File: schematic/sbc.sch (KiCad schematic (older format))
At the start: 15 parts

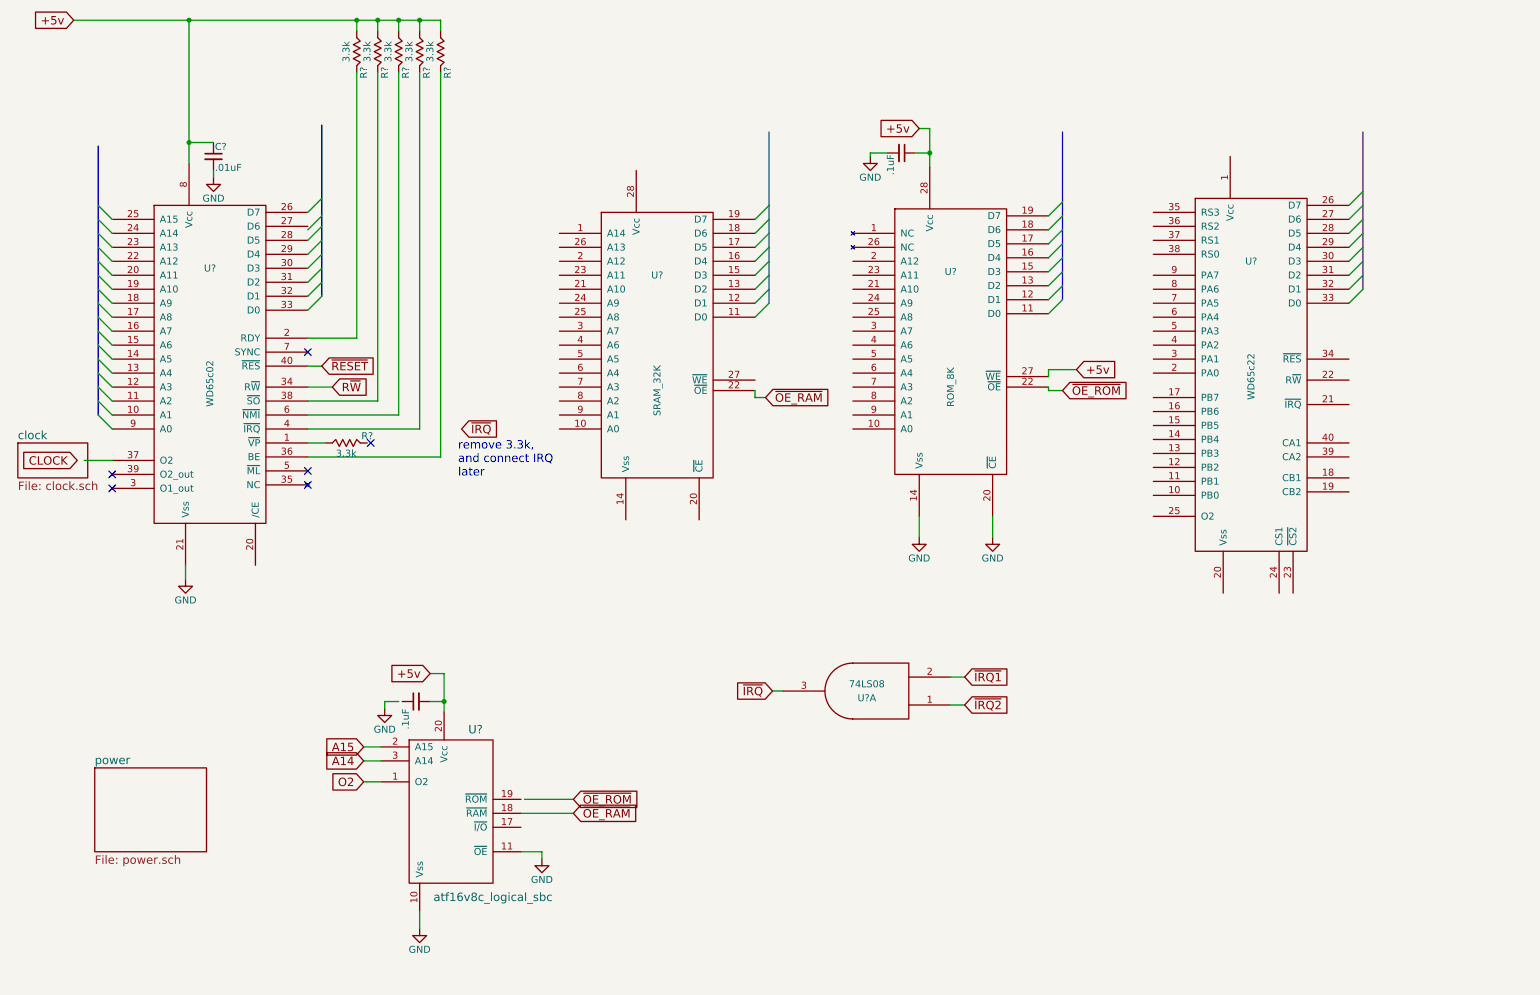
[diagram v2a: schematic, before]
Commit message: sbc schematic update. Wired in RAM
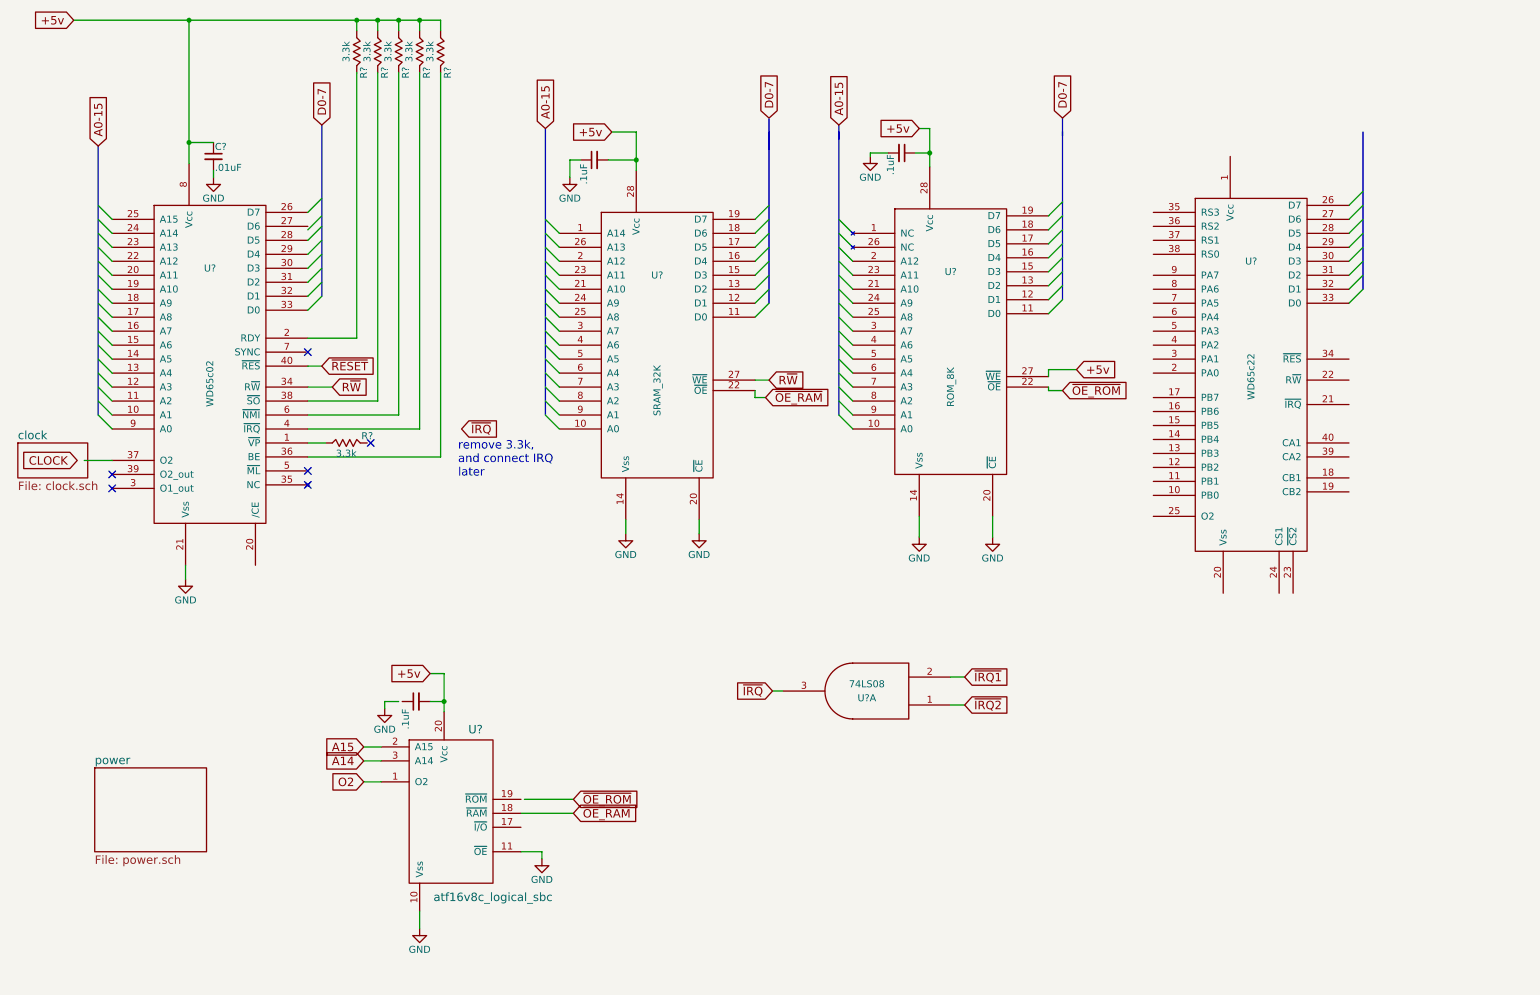
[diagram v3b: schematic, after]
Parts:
- added C?: .1uF, symbol C_Small
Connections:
- net labels added: A0-15, D0-7
- wire segments 53 -> 61
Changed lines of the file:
@@
 Text GLabel 5825 3475 2    60   Input ~ 0
 ~OE_RAM~
-Wire Bus Line
-	10100 1575 10100 2700
-Wire Bus Line
-	7950 1575 7950 2775
-Wire Bus Line
-	5850 1575 5850 2800
-Wire Bus Line
-	2650 1525 2650 2750
-Wire Wire Line
-	5875 5575 5950 5575
-Wire Wire Line
-	7150 5475 7250 5475
-Wire Wire Line
-	7150 5675 7250 5675
-Wire Wire Line
-	3350 3700 3350 1150
-Wire Wire Line
-	2550 3600 3200 3600
-Wire Wire Line
-	3200 3600 3200 1150
-Wire Wire Line
-	2550 3050 2900 3050
-Wire Wire Line
-	2550 3500 3050 3500
-Wire Wire Line
-	3050 3500 3050 1150
-Wire Wire Line
-	2550 3400 2725 3400
-Wire Wire Line
-	2550 3250 2650 3250
-Wire Wire Line
-	1700 1800 1700 775
-Wire Wire Line
-	875  775  3500 775
-Connection ~ 1700 775
-Wire Wire Line
-	2900 3050 2900 1150
-Wire Wire Line
-	3500 775  3500 850
-Wire Wire Line
-	3350 850  3350 775
-Connection ~ 3350 775
-Connection ~ 3200 775
-Wire Wire Line
-	3050 850  3050 775
-Connection ~ 3050 775
-Wire Wire Line
-	2900 850  2900 775
-Connection ~ 2900 775
-Wire Wire Line
-	3200 850  3200 775
-Wire Bus Line
-	1050 3600 1050 1675
-Wire Wire Line
-	950  3925 1150 3925
-Wire Wire Line
-	1675 4775 1675 4675
-Wire Wire Line
-	1875 1650 1700 1650
-Connection ~ 1700 1650
-Wire Wire Line
-	1875 1900 1875 1850
-Wire Wire Line
-	2550 3800 2675 3800
-Wire Wire Line
-	2550 3900 3500 3900
-Wire Wire Line
-	3500 3900 3500 1150
-Wire Wire Line
-	2550 3700 3350 3700
-Wire Wire Line
-	4100 6350 4450 6350
-Wire Wire Line
-	4075 6450 4450 6450
-Wire Wire Line
-	7950 3425 7850 3425
-Wire Wire Line
-	7850 3425 7850 3400
-Wire Wire Line
-	5750 3425 5750 3475
-Wire Wire Line
-	5750 3475 5825 3475
 $Comp
 L GND #PWR?
@@
 	1    0    0    -1
 $EndComp
-Wire Wire Line
-	3350 7275 3350 7150
-Wire Wire Line
-	4075 6725 4225 6725
-Wire Wire Line
-	4225 6725 4225 6775
 Text GLabel 3425 5450 0    60   Input ~ 0
 +5v
@@
 	0    -1   -1   0
 $EndComp
-Wire Wire Line
-	3425 5450 3525 5450
-Wire Wire Line
-	3525 5450 3525 5725
-Wire Wire Line
-	3425 5650 3525 5650
-Connection ~ 3525 5650
 $Comp
 L GND #PWR?
@@
 	1    0    0    -1
 $EndComp
-Wire Wire Line
-	3200 5650 3100 5650
-Wire Wire Line
-	3100 5650 3100 5700
 Text GLabel 2950 5975 0    60   Input ~ 0
 A15
 Text GLabel 2950 6075 0    60   Input ~ 0
 A14
-Wire Wire Line
-	2950 5975 3075 5975
-Wire Wire Line
-	2950 6075 3075 6075
 Text GLabel 2950 6225 0    60   Input ~ 0
 O2
-Wire Wire Line
-	2950 6225 3075 6225
 Text GLabel 6925 1550 0    60   Input ~ 0
 +5v
@@
 	1    0    0    -1
 $EndComp
-Wire Wire Line
-	6925 1550 7000 1550
-Wire Wire Line
-	7000 1550 7000 1825
-Wire Wire Line
-	6900 1725 7000 1725
-Connection ~ 7000 1725
-Wire Wire Line
-	6700 1725 6575 1725
-Wire Wire Line
-	6575 1725 6575 1750
 $Comp
 L GND #PWR?
@@
 	1    0    0    -1
 $EndComp
-Wire Wire Line
-	7450 4475 7450 4325
-Wire Wire Line
-	6925 4475 6925 4325
 Text GLabel 8050 3275 2    60   Input ~ 0
 +5v
+$Comp
+L GND #PWR?
+U 1 1 5830B7BE
+P 5350 4450
+F 0 "#PWR?" H 5350 4200 50  0001 C CNN
+F 1 "GND" H 5350 4300 50  0000 C CNN
+F 2 "" H 5350 4450 50  0000 C CNN
+F 3 "" H 5350 4450 50  0000 C CNN
+	1    5350 4450
+	1    0    0    -1
+$EndComp
+$Comp
+L GND #PWR?
+U 1 1 5830B7F9
+P 4825 4450
+F 0 "#PWR?" H 4825 4200 50  0001 C CNN
+F 1 "GND" H 4825 4300 50  0000 C CNN
+F 2 "" H 4825 4450 50  0000 C CNN
+F 3 "" H 4825 4450 50  0000 C CNN
+	1    4825 4450
+	1    0    0    -1
+$EndComp
+Text GLabel 5850 3350 2    60   Input ~ 0
+R~W~
+Text GLabel 4725 1575 0    60   Input ~ 0
++5v
+$Comp
+L C_Small C?
+U 1 1 5830BB33
+P 4600 1775
+F 0 "C?" H 4610 1845 50  0001 L CNN
+F 1 ".1uF" H 4425 1850 50  0000 L CNN
+F 2 "" H 4600 1775 50  0000 C CNN
+F 3 "" H 4600 1775 50  0000 C CNN
+	1    4600 1775
+	0    -1   -1   0
+$EndComp
+$Comp
+L GND #PWR?
+U 1 1 5830BC6D
+P 4425 1900
+F 0 "#PWR?" H 4425 1650 50  0001 C CNN
+F 1 "GND" H 4425 1750 50  0000 C CNN
+F 2 "" H 4425 1900 50  0000 C CNN
+F 3 "" H 4425 1900 50  0000 C CNN
+	1    4425 1900
+	1    0    0    -1
+$EndComp
+Entry Wire Line
+	4250 2200 4350 2300
+Entry Wire Line
+	4250 2300 4350 2400
+Entry Wire Line
+	4250 2400 4350 2500
+Entry Wire Line
+	4250 2500 4350 2600
+Entry Wire Line
+	4250 2600 4350 2700
+Entry Wire Line
+	4250 2700 4350 2800
+Entry Wire Line
+	4250 2800 4350 2900
+Entry Wire Line
+	4250 2900 4350 3000
+Entry Wire Line
+	4250 3000 4350 3100
+Entry Wire Line
+	4250 3100 4350 3200
+Entry Wire Line
+	4250 3200 4350 3300
+Entry Wire Line
+	4250 3300 4350 3400
+Entry Wire Line
+	4250 3400 4350 3500
+Entry Wire Line
+	4250 3500 4350 3600
+Entry Wire Line
+	4250 3600 4350 3700
+Entry Wire Line
+	6350 2200 6450 2300
+Entry Wire Line
+	6350 2300 6450 2400
+Entry Wire Line
+	6350 2400 6450 2500
+Entry Wire Line
+	6350 2500 6450 2600
+Entry Wire Line
+	6350 2600 6450 2700
+Entry Wire Line
+	6350 2700 6450 2800
+Entry Wire Line
+	6350 2800 6450 2900
+Entry Wire Line
+	6350 2900 6450 3000
+Entry Wire Line
+	6350 3000 6450 3100
+Entry Wire Line
+	6350 3100 6450 3200
+Entry Wire Line
+	6350 3200 6450 3300
+Entry Wire Line
+	6350 3300 6450 3400
+Entry Wire Line
+	6350 3400 6450 3500
+Entry Wire Line
+	6350 3500 6450 3600
+Entry Wire Line
+	6350 3600 6450 3700
+Text GLabel 6350 1525 1    60   Input ~ 0
+A0-15
+Text GLabel 4250 1550 1    60   Input ~ 0
+A0-15
+Text GLabel 1050 1675 1    60   Input ~ 0
+A0-15
+Text GLabel 5850 1475 1    60   Input ~ 0
+D0-7
+Text GLabel 7950 1475 1    60   Input ~ 0
+D0-7
+Text GLabel 2650 1525 1    60   Input ~ 0
+D0-7
+Wire Bus Line
+	10100 1575 10100 2700
+Wire Bus Line
+	7950 1575 7950 2775
+Wire Bus Line
+	5850 1575 5850 2800
+Wire Bus Line
+	2650 1525 2650 2750
+Wire Wire Line
+	5875 5575 5950 5575
+Wire Wire Line
+	7150 5475 7250 5475
+Wire Wire Line
+	7150 5675 7250 5675
+Wire Wire Line
+	3350 3700 3350 1150
+Wire Wire Line
+	2550 3600 3200 3600
+Wire Wire Line
+	3200 3600 3200 1150
+Wire Wire Line
+	2550 3050 2900 3050
+Wire Wire Line
+	2550 3500 3050 3500
+Wire Wire Line
+	3050 3500 3050 1150
+Wire Wire Line
+	2550 3400 2725 3400
+Wire Wire Line
+	2550 3250 2650 3250
+Wire Wire Line
+	1700 1800 1700 775
+Wire Wire Line
+	875  775  3500 775
+Connection ~ 1700 775
+Wire Wire Line
+	2900 3050 2900 1150
+Wire Wire Line
+	3500 775  3500 850
+Wire Wire Line
+	3350 850  3350 775
+Connection ~ 3350 775
+Connection ~ 3200 775
+Wire Wire Line
+	3050 850  3050 775
+Connection ~ 3050 775
+Wire Wire Line
+	2900 850  2900 775
+Connection ~ 2900 775
+Wire Wire Line
+	3200 850  3200 775
+Wire Bus Line
+	1050 3600 1050 1675
+Wire Wire Line
+	950  3925 1150 3925
+Wire Wire Line
+	1675 4775 1675 4675
+Wire Wire Line
+	1875 1650 1700 1650
+Connection ~ 1700 1650
+Wire Wire Line
+	1875 1900 1875 1850
+Wire Wire Line
+	2550 3800 2675 3800
+Wire Wire Line
+	2550 3900 3500 3900
+Wire Wire Line
+	3500 3900 3500 1150
+Wire Wire Line
+	2550 3700 3350 3700
+Wire Wire Line
+	4100 6350 4450 6350
+Wire Wire Line
+	4075 6450 4450 6450
+Wire Wire Line
+	7950 3425 7850 3425
+Wire Wire Line
+	7850 3425 7850 3400
+Wire Wire Line
+	5750 3425 5750 3475
+Wire Wire Line
+	5750 3475 5825 3475
+Wire Wire Line
+	3350 7275 3350 7150
+Wire Wire Line
+	4075 6725 4225 6725
+Wire Wire Line
+	4225 6725 4225 6775
+Wire Wire Line
+	3425 5450 3525 5450
+Wire Wire Line
+	3525 5450 3525 5725
+Wire Wire Line
+	3425 5650 3525 5650
+Connection ~ 3525 5650
+Wire Wire Line
+	3200 5650 3100 5650
+Wire Wire Line
+	3100 5650 3100 5700
+Wire Wire Line
+	2950 5975 3075 5975
+Wire Wire Line
+	2950 6075 3075 6075
+Wire Wire Line
+	2950 6225 3075 6225
+Wire Wire Line
+	6925 1550 7000 1550
+Wire Wire Line
+	7000 1550 7000 1825
+Wire Wire Line
+	6900 1725 7000 1725
+Connection ~ 7000 1725
+Wire Wire Line
+	6700 1725 6575 1725
+Wire Wire Line
+	6575 1725 6575 1750
+Wire Wire Line
+	7450 4475 7450 4325
+Wire Wire Line
+	6925 4475 6925 4325
 Wire Wire Line
 	7850 3325 7850 3275
 Wire Wire Line
 	7850 3275 8050 3275
+Wire Wire Line
+	5350 4450 5350 4350
+Wire Wire Line
+	4825 4450 4825 4350
+Wire Wire Line
+	5750 3350 5850 3350
+Wire Wire Line
+	4725 1575 4900 1575
+Wire Wire Line
+	4900 1575 4900 1850
+Wire Wire Line
+	4700 1775 4900 1775
+Connection ~ 4900 1775
+Wire Bus Line
+	6350 3600 6350 1575
+Wire Wire Line
+	4425 1900 4425 1775
+Wire Wire Line
+	4425 1775 4500 1775
+Wire Bus Line
+	4250 3600 4250 1550
+Wire Bus Line
+	6350 1525 6350 1625
+Wire Bus Line
+	5850 1475 5850 1700
+Wire Bus Line
+	7950 1475 7950 1600
 $EndSCHEMATC

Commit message: Added 65c22 basic connections to schematic
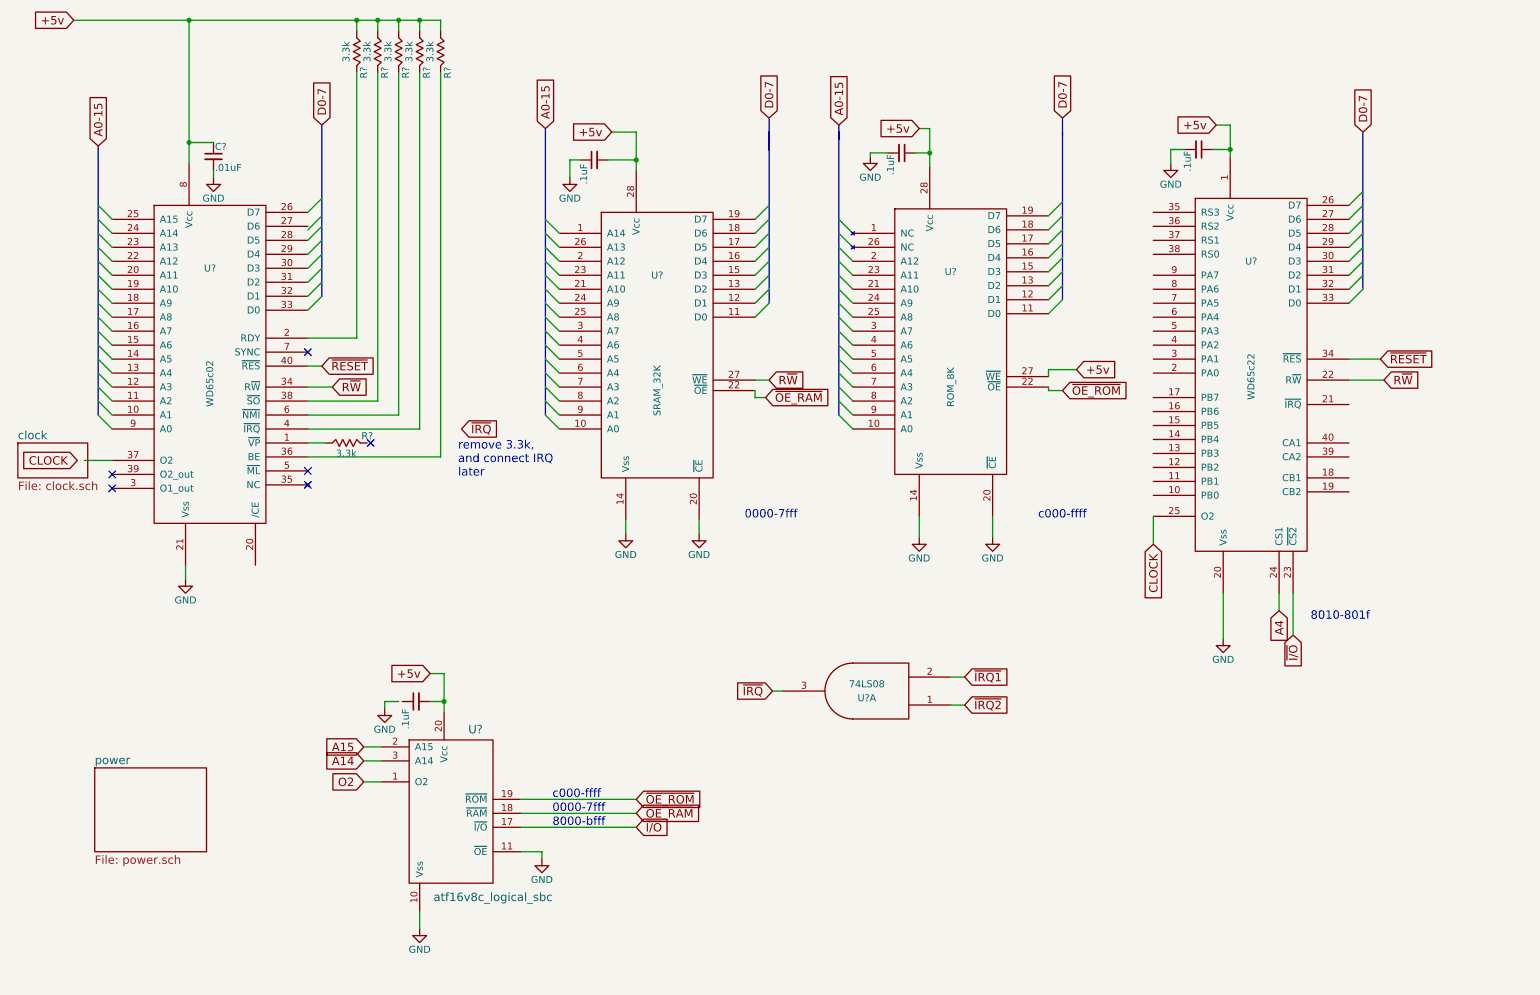
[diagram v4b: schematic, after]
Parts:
- added C?: .1uF, symbol C_Small
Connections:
- net labels added: A4, ~I/O~
- wire segments 61 -> 73
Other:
- note added: "0000-7fff"
- note added: "8000-bfff"
- note added: "8010-801f"
- note added: "c000-ffff"
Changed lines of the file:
@@
 	1    0    0    -1
 $EndComp
-Text GLabel 4450 6350 2    60   Input ~ 0
+Text GLabel 4900 6350 2    60   Input ~ 0
 ~OE_ROM~
-Text GLabel 4450 6450 2    60   Input ~ 0
+Text GLabel 4900 6450 2    60   Input ~ 0
 ~OE_RAM~
 Text GLabel 7950 3425 2    60   Input ~ 0
@@
 	2550 3700 3350 3700
 Wire Wire Line
-	4100 6350 4450 6350
-Wire Wire Line
-	4075 6450 4450 6450
+	4075 6450 4900 6450
 Wire Wire Line
 	7950 3425 7850 3425
@@
 Wire Bus Line
 	7950 1475 7950 1600
+Text GLabel 9500 5000 3    60   Input ~ 0
+A4
+Wire Wire Line
+	9500 5000 9500 4875
+Text GLabel 9600 5175 3    60   Input ~ 0
+~I/O~
+Wire Wire Line
+	9600 5175 9600 4875
+Text GLabel 4900 6550 2    60   Input ~ 0
+~I/O~
+Wire Wire Line
+	4075 6550 4900 6550
+Wire Wire Line
+	4075 6350 4900 6350
+Text Notes 9725 5075 0    60   ~ 0
+8010-801f
+Text Notes 7775 4350 0    60   ~ 0
+c000-ffff
+Text Notes 5675 4350 0    60   ~ 0
+0000-7fff
+Text Notes 4300 6350 0    60   ~ 0
+c000-ffff
+Text Notes 4300 6450 0    60   ~ 0
+0000-7fff
+Text Notes 4300 6550 0    60   ~ 0
+8000-bfff
+$Comp
+L GND #PWR?
+U 1 1 58336CFD
+P 9100 5200
+F 0 "#PWR?" H 9100 4950 50  0001 C CNN
+F 1 "GND" H 9100 5050 50  0000 C CNN
+F 2 "" H 9100 5200 50  0000 C CNN
+F 3 "" H 9100 5200 50  0000 C CNN
+	1    9100 5200
+	1    0    0    -1
+$EndComp
+Wire Wire Line
+	9100 4875 9100 5200
+Text GLabel 9050 1525 0    60   Input ~ 0
++5v
+$Comp
+L GND #PWR?
+U 1 1 58336E6C
+P 8725 1800
+F 0 "#PWR?" H 8725 1550 50  0001 C CNN
+F 1 "GND" H 8725 1650 50  0000 C CNN
+F 2 "" H 8725 1800 50  0000 C CNN
+F 3 "" H 8725 1800 50  0000 C CNN
+	1    8725 1800
+	1    0    0    -1
+$EndComp
+$Comp
+L C_Small C?
+U 1 1 58336E9A
+P 8925 1700
+F 0 "C?" H 8935 1770 50  0001 L CNN
+F 1 ".1uF" H 8935 1620 50  0000 L CNN
+F 2 "" H 8925 1700 50  0000 C CNN
+F 3 "" H 8925 1700 50  0000 C CNN
+	1    8925 1700
+	0    1    1    0
+$EndComp
+Wire Wire Line
+	9025 1700 9150 1700
+Wire Wire Line
+	9150 1525 9150 1750
+Wire Wire Line
+	9150 1525 9050 1525
+Connection ~ 9150 1700
+Wire Wire Line
+	8725 1800 8725 1700
+Wire Wire Line
+	8725 1700 8825 1700
+Text GLabel 10100 1575 1    60   Input ~ 0
+D0-7
+Text GLabel 10250 3350 2    60   Input ~ 0
+R~W~
+Text GLabel 10225 3200 2    60   Input ~ 0
+~RESET~
+Text GLabel 8600 4525 3    60   Input ~ 0
+CLOCK
+Wire Wire Line
+	10000 3200 10225 3200
+Wire Wire Line
+	10000 3350 10250 3350
+Wire Wire Line
+	8600 4525 8600 4325
 $EndSCHEMATC
